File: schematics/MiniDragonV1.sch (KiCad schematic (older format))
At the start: 0 parts

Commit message: Update block diagrams to reflect a more complete layout.
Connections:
- no-connect marks 0 -> 3

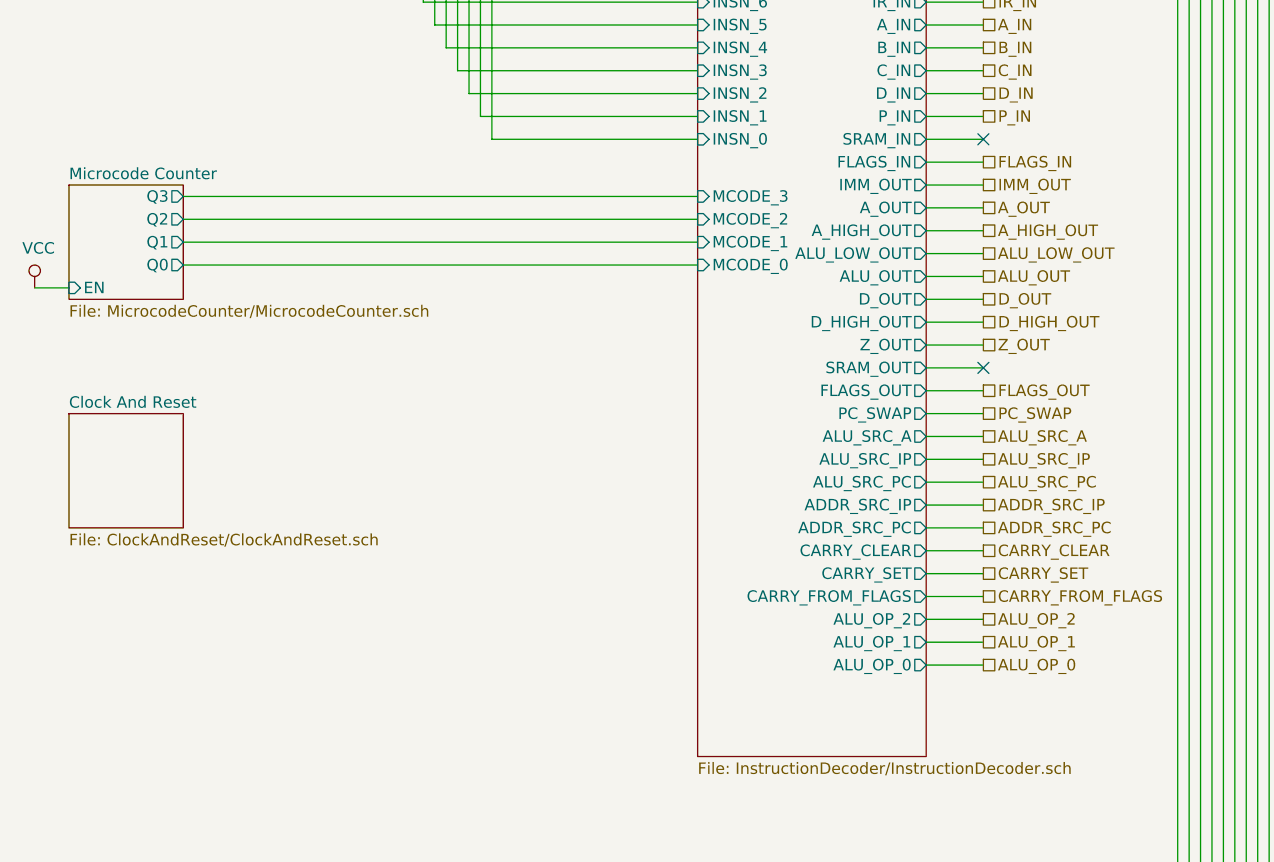
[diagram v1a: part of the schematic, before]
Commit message: Update schematics to reflect Rev.2 AND/OR circuits now that they're tested, incorporate microcode ability to end instruction decoding early.
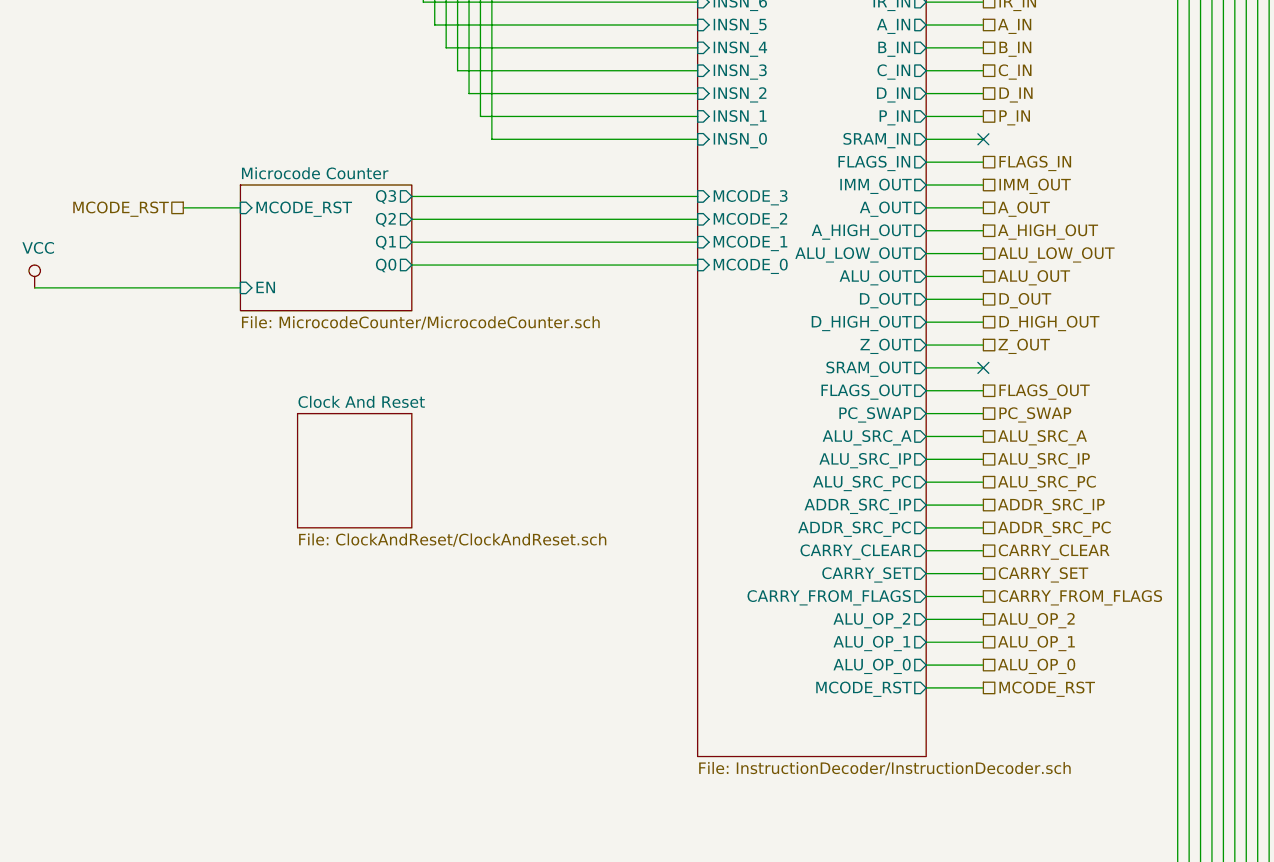
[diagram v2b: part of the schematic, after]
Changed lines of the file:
@@
 $Descr A0 46811 33110
 encoding utf-8
-Sheet 1 372
+Sheet 1 373
 Title "MiniDragon Block Diagram"
 Date "2020-03-02"
@@
 $EndSheet
 $Sheet
-S 1000 16000 500  500
+S 2000 16000 500  500
 U 5E5DE44B
 F0 "Clock And Reset" 50
@@
 $EndSheet
 $Sheet
-S 1000 15000 500  500
+S 1750 15000 750  550
 U 5E60328A
 F0 "Microcode Counter" 50
 F1 "MicrocodeCounter/MicrocodeCounter.sch" 50
-F2 "EN" I L 1000 15450 50
-F3 "Q0" O R 1500 15350 50
-F4 "Q1" O R 1500 15250 50
-F5 "Q2" O R 1500 15150 50
-F6 "Q3" O R 1500 15050 50
+F2 "EN" I L 1750 15450 50
+F3 "Q0" O R 2500 15350 50
+F4 "Q1" O R 2500 15250 50
+F5 "Q2" O R 2500 15150 50
+F6 "Q3" O R 2500 15050 50
+F7 "MCODE_RST" I L 1750 15100 50
 $EndSheet
 $Comp
@@
 $EndComp
 Wire Wire Line
-	850  15450 1000 15450
+	850  15450 1750 15450
 Wire Wire Line
 	6600 4000 6600 2300
@@
 	8000 14900 8200 14900
 Wire Wire Line
-	1500 15050 3750 15050
-Wire Wire Line
-	3750 15150 1500 15150
-Wire Wire Line
-	1500 15250 3750 15250
-Wire Wire Line
-	3750 15350 1500 15350
+	2500 15050 3750 15050
+Wire Wire Line
+	3750 15150 2500 15150
+Wire Wire Line
+	2500 15250 3750 15250
+Wire Wire Line
+	3750 15350 2500 15350
 Wire Wire Line
 	2850 13450 2850 14800
@@
 F43 "ALU_OP_1" O R 4750 17000 50
 F44 "ALU_OP_0" O R 4750 17100 50
+F45 "MCODE_RST" O R 4750 17200 50
 $EndSheet
 Text HLabel 5000 14100 2    50   UnSpc ~ 0
@@
 Text HLabel 3550 1350 0    50   UnSpc ~ 0
 PC_SWAP
+Text HLabel 5000 17200 2    50   UnSpc ~ 0
+MCODE_RST
+Wire Wire Line
+	4750 17200 5000 17200
+Text HLabel 1500 15100 0    50   UnSpc ~ 0
+MCODE_RST
+Wire Wire Line
+	1500 15100 1750 15100
 $EndSCHEMATC

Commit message: Major addition to schematics:
 - Block diagram of U/V registers.
 - Initial block diagrams of RAM interface.
 - Patch buffers to clock and instruction decoder.
 - Microcode counter now has a cycle for load instruction microcode.
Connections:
- no-connect marks 3 -> 1

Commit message: Update schematics to match work done with inverted MCODE_RST and a few other tweaks.
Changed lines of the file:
@@
 $Descr A0 46811 33110
 encoding utf-8
-Sheet 1 478
+Sheet 1 479
 Title "MiniDragon Block Diagram"
 Date "2020-03-02"
@@
 F4 "Q2" O R 2500 15150 50
 F5 "Q3" O R 2500 15050 50
-F6 "MCODE_RST" I L 1750 15100 50
-F7 "ILOAD" O R 2500 15500 50
+F6 "~MCODE_RST" I L 1750 15100 50
+F7 "~ILOAD" O R 2500 15500 50
 $EndSheet
 Wire Wire Line
@@
 PC_SWAP
 Text HLabel 5000 18400 2    50   UnSpc ~ 0
-MCODE_RST
+~MCODE_RST
 Text HLabel 1500 15100 0    50   UnSpc ~ 0
-MCODE_RST
+~MCODE_RST
 Wire Wire Line
 	1500 15100 1750 15100
@@
 F42 "ALU_OP_1" O R 4750 17000 50
 F43 "ALU_OP_0" O R 4750 17100 50
-F44 "MCODE_RST" O R 4750 18400 50
-F45 "IMM_4_OUT" O R 4750 17300 50
-F46 "IMM_6_OUT" O R 4750 17400 50
-F47 "U_OUT" O R 4750 17700 50
-F48 "V_OUT" O R 4750 17800 50
-F49 "U_IN" O R 4750 17900 50
-F50 "V_IN" O R 4750 18000 50
-F51 "~ILOAD" I L 3750 15500 50
+F44 "IMM_4_OUT" O R 4750 17300 50
+F45 "IMM_6_OUT" O R 4750 17400 50
+F46 "U_OUT" O R 4750 17700 50
+F47 "V_OUT" O R 4750 17800 50
+F48 "U_IN" O R 4750 17900 50
+F49 "V_IN" O R 4750 18000 50
+F50 "~ILOAD" I L 3750 15500 50
+F51 "~MCODE_RST" O R 4750 18400 50
 $EndSheet
 Text HLabel 5000 14800 2    50   UnSpc ~ 0
